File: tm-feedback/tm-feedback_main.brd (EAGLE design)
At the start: 100 x 80 mm, 51 parts

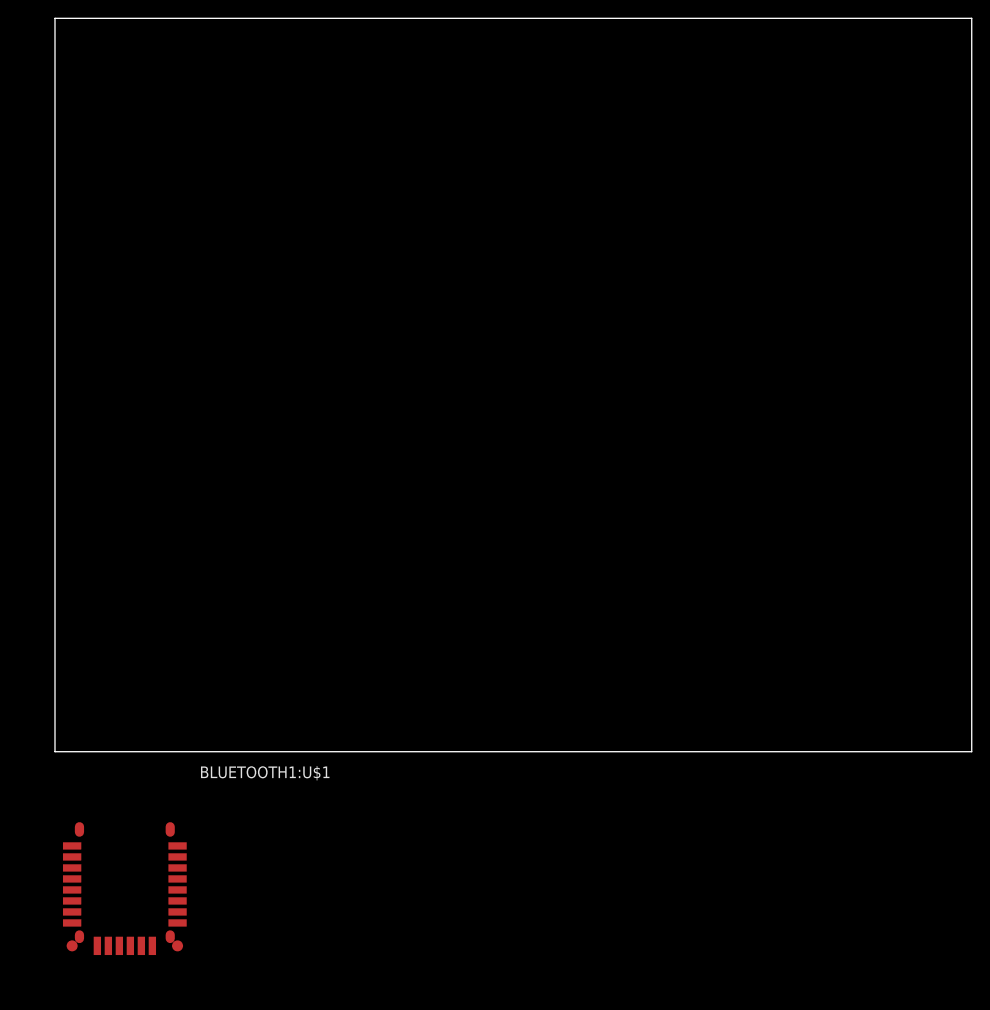
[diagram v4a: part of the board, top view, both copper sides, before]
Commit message: Moved Bluetooth Module to rigth place
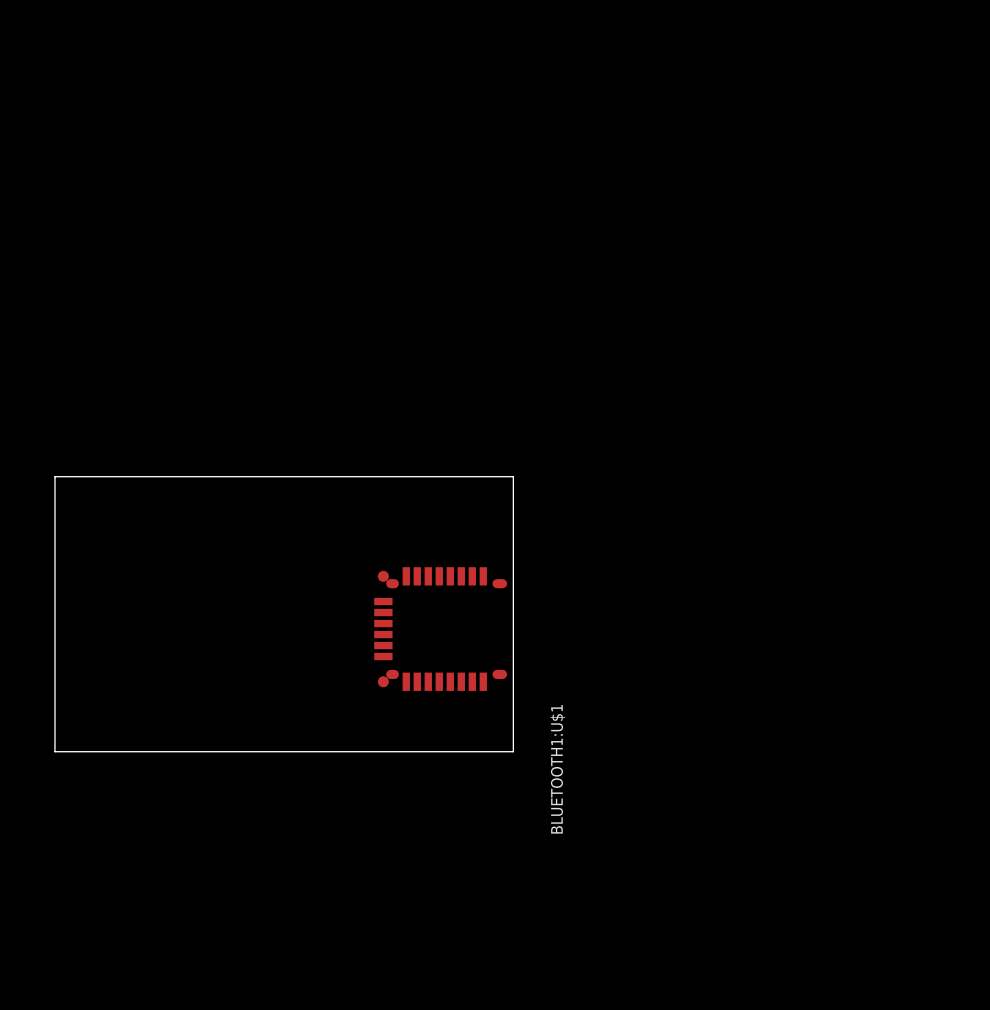
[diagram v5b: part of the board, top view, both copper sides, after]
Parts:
- moved BLUETOOTH1:U$1 45.3 mm to (45.6, 13.4), turned to 270 degrees
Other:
- board size 100 x 80 mm -> 50 x 30 mm
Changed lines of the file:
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@@
 <setting verticaltext="up"/>
 </settings>
-<grid distance="0.05" unitdist="inch" unit="inch" style="lines" multiple="1" display="no" altdistance="0.025" altunitdist="inch" altunit="inch"/>
+<grid distance="1" unitdist="mm" unit="mm" style="lines" multiple="1" display="yes" altdistance="0.1" altunitdist="mm" altunit="mm"/>
 <layers>
 <layer number="1" name="Top" color="4" fill="1" visible="yes" active="yes"/>
@@
 <board>
 <plain>
-<wire x1="0" y1="0" x2="100" y2="0" width="0" layer="20"/>
-<wire x1="100" y1="0" x2="100" y2="80" width="0" layer="20"/>
-<wire x1="100" y1="80" x2="0" y2="80" width="0" layer="20"/>
-<wire x1="0" y1="80" x2="0" y2="0" width="0" layer="20"/>
+<wire x1="0" y1="0" x2="50" y2="0" width="0" layer="20"/>
+<wire x1="50" y1="0" x2="50" y2="30" width="0" layer="20"/>
+<wire x1="50" y1="30" x2="0" y2="30" width="0" layer="20"/>
+<wire x1="0" y1="30" x2="0" y2="0" width="0" layer="20"/>
 </plain>
 <attributes>
@@
 </autorouter>
 <elements>
-<element name="BLUETOOTH1:U$1" library="tactile-music" package="RN4020" value="RN4020" x="7.62" y="-11.43"/>
+<element name="BLUETOOTH1:U$1" library="tactile-music" package="RN4020" value="RN4020" x="45.57" y="13.38" rot="R270"/>
 <element name="POWER_SUPPLY1:LED1" library="led" package="CHIPLED_0805" value="RED" x="-16.51" y="-62.23"/>
 <element name="POWER_SUPPLY1:R1" library="resistor" package="R0805" value="60" x="-16.51" y="-68.58"/>
@@
 <wire x1="-53.34" y1="-118.11" x2="-60.96" y2="-132.08" width="0" layer="19" extent="1-1"/>
 <wire x1="-17.46" y1="-68.58" x2="-53.34" y2="-118.11" width="0" layer="19" extent="1-1"/>
-<wire x1="1.87" y1="-21.18" x2="-17.46" y2="-68.58" width="0" layer="19" extent="1-1"/>
-<wire x1="1.87" y1="-10.28" x2="1.87" y2="-21.18" width="0" layer="19" extent="1-1"/>
-<wire x1="13.37" y1="-21.18" x2="1.87" y2="-21.18" width="0" layer="19" extent="1-1"/>
-<wire x1="13.37" y1="-10.28" x2="13.37" y2="-21.18" width="0" layer="19" extent="1-1"/>
+<wire x1="35.82" y1="7.63" x2="-17.46" y2="-68.58" width="0" layer="19" extent="1-1"/>
+<wire x1="46.72" y1="7.63" x2="35.82" y2="7.63" width="0" layer="19" extent="1-1"/>
+<wire x1="46.72" y1="19.13" x2="46.72" y2="7.63" width="0" layer="19" extent="1-1"/>
+<wire x1="35.82" y1="19.13" x2="46.72" y2="19.13" width="0" layer="19" extent="1-1"/>
 </signal>
 <signal name="BLUETOOTH1:N$6">
@@
 <wire x1="-92.39" y1="-267.97" x2="-92.39" y2="-255.27" width="0" layer="19" extent="1-1"/>
 <wire x1="-92.39" y1="-274.32" x2="-92.39" y2="-267.97" width="0" layer="19" extent="1-1"/>
-<wire x1="13.37" y1="-11.48" x2="-28.26" y2="-83.82" width="0" layer="19" extent="1-1"/>
+<wire x1="45.52" y1="7.63" x2="-28.26" y2="-83.82" width="0" layer="19" extent="1-1"/>
 <wire x1="-96.84" y1="-421.64" x2="-92.39" y2="-274.32" width="0" layer="19" extent="1-1"/>
 <wire x1="-96.84" y1="-426.72" x2="-96.84" y2="-421.64" width="0" layer="19" extent="1-1"/>
@@
 <contactref element="BLUETOOTH1:U$1" pad="14"/>
 <contactref element="MICROCONTROLLER1:U1" pad="27"/>
-<wire x1="9.42" y1="-21.18" x2="-81.93" y2="-234.48" width="0" layer="19" extent="1-1"/>
+<wire x1="35.82" y1="11.58" x2="-81.93" y2="-234.48" width="0" layer="19" extent="1-1"/>
 </signal>
 <signal name="N$6">
 <contactref element="BLUETOOTH1:U$1" pad="18"/>
 <contactref element="MICROCONTROLLER1:U1" pad="41"/>
-<wire x1="13.37" y1="-17.48" x2="-89.23" y2="-227.98" width="0" layer="19" extent="1-1"/>
+<wire x1="39.52" y1="7.63" x2="-89.23" y2="-227.98" width="0" layer="19" extent="1-1"/>
 </signal>
 <signal name="N$7">
 <contactref element="BLUETOOTH1:U$1" pad="5"/>
 <contactref element="MICROCONTROLLER1:U1" pad="5"/>
-<wire x1="1.87" y1="-15.08" x2="-93.33" y2="-232.88" width="0" layer="19" extent="1-1"/>
+<wire x1="41.92" y1="19.13" x2="-93.33" y2="-232.88" width="0" layer="19" extent="1-1"/>
 </signal>
 <signal name="N$8">
 <contactref element="BLUETOOTH1:U$1" pad="6"/>
 <contactref element="MICROCONTROLLER1:U1" pad="4"/>
-<wire x1="1.87" y1="-16.28" x2="-93.33" y2="-232.08" width="0" layer="19" extent="1-1"/>
+<wire x1="40.72" y1="19.13" x2="-93.33" y2="-232.08" width="0" layer="19" extent="1-1"/>
 </signal>
 <signal name="N$9">
 <contactref element="BLUETOOTH1:U$1" pad="15"/>
 <contactref element="MICROCONTROLLER1:U1" pad="38"/>
-<wire x1="10.62" y1="-21.18" x2="-86.83" y2="-227.98" width="0" layer="19" extent="1-1"/>
+<wire x1="35.82" y1="10.38" x2="-86.83" y2="-227.98" width="0" layer="19" extent="1-1"/>
 </signal>
 <signal name="N$10">
@@
 <contactref element="MICROCONTROLLER1:U1" pad="3"/>
 <wire x1="-93.33" y1="-231.28" x2="-70.17" y2="-184.15" width="0" layer="19" extent="1-1"/>
-<wire x1="1.87" y1="-17.48" x2="-70.17" y2="-184.15" width="0" layer="19" extent="1-1"/>
+<wire x1="39.52" y1="19.13" x2="-70.17" y2="-184.15" width="0" layer="19" extent="1-1"/>
 </signal>
 <signal name="N$11">
 <contactref element="BLUETOOTH1:U$1" pad="8"/>
 <contactref element="MICROCONTROLLER1:U1" pad="2"/>
-<wire x1="1.87" y1="-18.68" x2="-93.33" y2="-230.48" width="0" layer="19" extent="1-1"/>
+<wire x1="38.32" y1="19.13" x2="-93.33" y2="-230.48" width="0" layer="19" extent="1-1"/>
 </signal>
 <signal name="N$12">
@@
 <contactref element="MICROCONTROLLER1:U1" pad="44"/>
 <wire x1="-70.17" y1="-189.23" x2="-91.63" y2="-227.98" width="0" layer="19" extent="1-1"/>
-<wire x1="4.62" y1="-21.18" x2="-70.17" y2="-189.23" width="0" layer="19" extent="1-1"/>
+<wire x1="35.82" y1="16.38" x2="-70.17" y2="-189.23" width="0" layer="19" extent="1-1"/>
 </signal>
 <signal name="N$13">
@@
 <contactref element="MICROCONTROLLER1:U1" pad="43"/>
 <wire x1="-76.52" y1="-212.09" x2="-90.83" y2="-227.98" width="0" layer="19" extent="1-1"/>
-<wire x1="5.82" y1="-21.18" x2="-76.52" y2="-212.09" width="0" layer="19" extent="1-1"/>
+<wire x1="35.82" y1="15.18" x2="-76.52" y2="-212.09" width="0" layer="19" extent="1-1"/>
 </signal>
 <signal name="N$14">
@@
 <contactref element="MICROCONTROLLER1:U1" pad="42"/>
 <wire x1="-76.52" y1="-234.95" x2="-90.03" y2="-227.98" width="0" layer="19" extent="1-1"/>
-<wire x1="7.02" y1="-21.18" x2="-90.03" y2="-227.98" width="0" layer="19" extent="1-1"/>
+<wire x1="35.82" y1="13.98" x2="-90.03" y2="-227.98" width="0" layer="19" extent="1-1"/>
 </signal>
 <signal name="N$4">

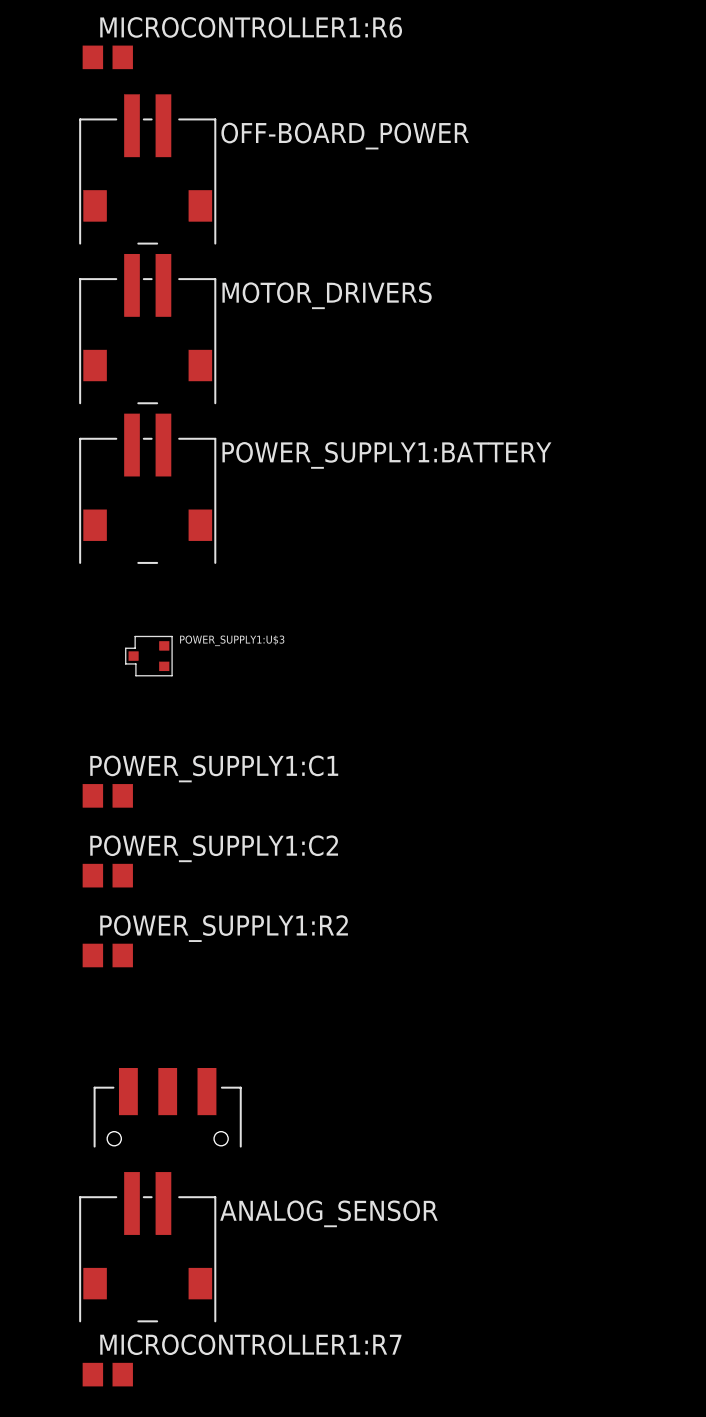
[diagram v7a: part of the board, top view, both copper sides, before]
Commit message: Replaced JST with picoblade
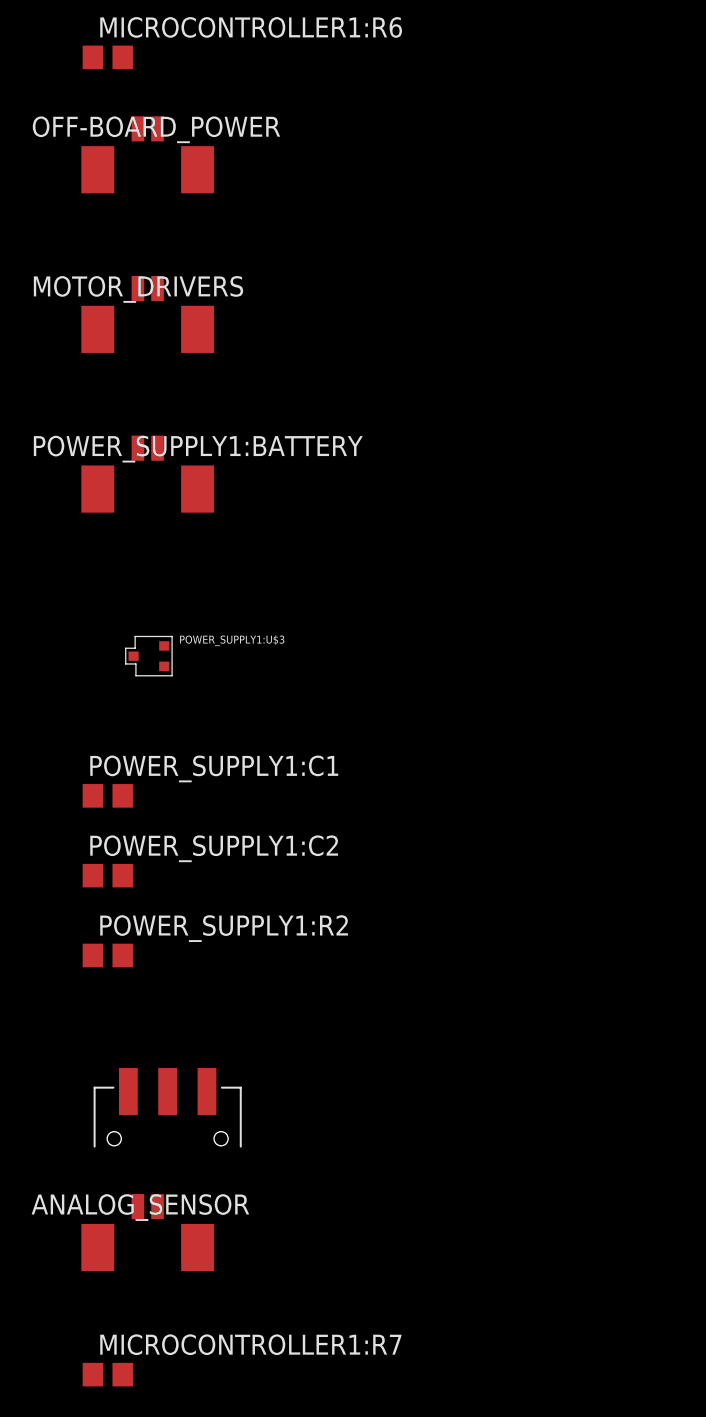
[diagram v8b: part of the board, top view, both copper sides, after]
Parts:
- ANALOG_SENSOR, MOTOR_DRIVERS, OFF-BOARD_POWER, POWER_SUPPLY1:BATTERY: value JST-SMD-2 -> PICOBLADE; device tactile-music:JST-SMD-2 -> tactile-music:PICOBLADE
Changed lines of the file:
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@@
 <element name="MICROCONTROLLER1:LED1" library="led" package="CHIPLED_0805" value="GREEN" x="-92.71" y="-359.41"/>
 <element name="MICROCONTROLLER1:R6" library="resistor" package="R0805" value="60Ω" x="-97.79" y="-369.57"/>
-<element name="OFF-BOARD_POWER" library="tactile-music" package="JST-SMD-2" value="JST-SMD-2" x="-95.25" y="-375.92"/>
-<element name="MOTOR_DRIVERS" library="tactile-music" package="JST-SMD-2" value="JST-SMD-2" x="-95.25" y="-386.08"/>
-<element name="POWER_SUPPLY1:BATTERY" library="tactile-music" package="JST-SMD-2" value="JST-SMD-2" x="-95.25" y="-396.24"/>
+<element name="OFF-BOARD_POWER" library="tactile-music" package="PICOBLADE" value="PICOBLADE" x="-95.25" y="-375.92"/>
+<element name="MOTOR_DRIVERS" library="tactile-music" package="PICOBLADE" value="PICOBLADE" x="-95.25" y="-386.08"/>
+<element name="POWER_SUPPLY1:BATTERY" library="tactile-music" package="PICOBLADE" value="PICOBLADE" x="-95.25" y="-396.24"/>
 <element name="POWER_SUPPLY1:U$3" library="tactile-music" package="SOT323(SC-70)" value="PMF370XN" x="-95.25" y="-407.67"/>
 <element name="POWER_SUPPLY1:C1" library="rcl" package="C0805" value="" x="-97.79" y="-416.56"/>
@@
 <element name="POWER_SUPPLY1:R2" library="resistor" package="R0805" value="60" x="-97.79" y="-426.72"/>
 <element name="POWER_SUPPLY1:POWER_SW" library="tactile-music" package="JS102011SAQN" value="JS102011SAQN" x="-93.98" y="-436.88"/>
-<element name="ANALOG_SENSOR" library="tactile-music" package="JST-SMD-2" value="JST-SMD-2" x="-95.25" y="-444.5"/>
+<element name="ANALOG_SENSOR" library="tactile-music" package="PICOBLADE" value="PICOBLADE" x="-95.25" y="-444.5"/>
 <element name="MICROCONTROLLER1:R7" library="resistor" package="R0805" value="10kΩ" x="-97.79" y="-453.39"/>
 <element name="MICROCONTROLLER1:R8" library="resistor" package="R0805" value="10kΩ" x="-97.79" y="-459.74"/>
@@
 <wire x1="-96.84" y1="-459.74" x2="-96.84" y2="-453.39" width="0" layer="19" extent="1-1"/>
 <wire x1="-96.84" y1="-466.09" x2="-96.84" y2="-459.74" width="0" layer="19" extent="1-1"/>
-<wire x1="-94.25" y1="-373.92" x2="-96.15" y2="-407.67" width="0" layer="19" extent="1-1"/>
-<wire x1="-92.71" y1="-358.36" x2="-94.25" y2="-373.92" width="0" layer="19" extent="1-1"/>
+<wire x1="-94.625" y1="-374.12" x2="-96.15" y2="-407.67" width="0" layer="19" extent="1-1"/>
+<wire x1="-92.71" y1="-358.36" x2="-94.625" y2="-374.12" width="0" layer="19" extent="1-1"/>
 <wire x1="-97.79" y1="-358.36" x2="-92.71" y2="-358.36" width="0" layer="19" extent="1-1"/>
 <wire x1="-97.79" y1="-327.88" x2="-97.79" y2="-358.36" width="0" layer="19" extent="1-1"/>
@@
 <contactref element="MOTOR_DRIVERS" pad="1"/>
 <contactref element="MICROCONTROLLER1:U1" pad="10"/>
-<wire x1="-93.33" y1="-236.88" x2="-96.25" y2="-384.08" width="0" layer="19" extent="1-1"/>
+<wire x1="-93.33" y1="-236.88" x2="-95.875" y2="-384.28" width="0" layer="19" extent="1-1"/>
 </signal>
 <signal name="N$5">
@@
 <contactref element="POWER_SUPPLY1:U$1" pad="1"/>
 <contactref element="POWER_SUPPLY1:POWER_SW" pad="3"/>
-<wire x1="-96.84" y1="-416.56" x2="-96.25" y2="-373.92" width="0" layer="19" extent="1-1"/>
+<wire x1="-96.84" y1="-416.56" x2="-95.875" y2="-374.12" width="0" layer="19" extent="1-1"/>
 <wire x1="-91.48" y1="-435.38" x2="-96.84" y2="-416.56" width="0" layer="19" extent="1-1"/>
-<wire x1="-59.7916" y1="-138.7602" x2="-96.25" y2="-373.92" width="0" layer="19" extent="1-1"/>
+<wire x1="-59.7916" y1="-138.7602" x2="-95.875" y2="-374.12" width="0" layer="19" extent="1-1"/>
 <wire x1="-16.51" y1="-63.28" x2="-59.7916" y2="-138.7602" width="0" layer="19" extent="1-1"/>
 </signal>
@@
 <contactref element="POWER_SUPPLY1:U$3" pad="1"/>
 <contactref element="POWER_SUPPLY1:POWER_SW" pad="2"/>
-<wire x1="-94.25" y1="-394.24" x2="-94.2" y2="-408.32" width="0" layer="19" extent="1-1"/>
+<wire x1="-94.625" y1="-394.44" x2="-94.2" y2="-408.32" width="0" layer="19" extent="1-1"/>
 <wire x1="-93.98" y1="-435.38" x2="-94.2" y2="-408.32" width="0" layer="19" extent="1-1"/>
 </signal>
@@
 <contactref element="POWER_SUPPLY1:BATTERY" pad="1"/>
 <contactref element="POWER_SUPPLY1:U$3" pad="2"/>
-<wire x1="-96.25" y1="-394.24" x2="-94.2" y2="-407.02" width="0" layer="19" extent="1-1"/>
+<wire x1="-95.875" y1="-394.44" x2="-94.2" y2="-407.02" width="0" layer="19" extent="1-1"/>
 </signal>
 <signal name="+3V3">
@@
 <contactref element="MICROCONTROLLER1:U1" pad="8"/>
 <contactref element="MOTOR_DRIVERS" pad="2"/>
-<wire x1="-93.33" y1="-235.28" x2="-94.25" y2="-384.08" width="0" layer="19" extent="1-1"/>
+<wire x1="-93.33" y1="-235.28" x2="-94.625" y2="-384.28" width="0" layer="19" extent="1-1"/>
 </signal>
 <signal name="N$15">
 <contactref element="ANALOG_SENSOR" pad="1"/>
 <contactref element="MICROCONTROLLER1:U1" pad="23"/>
-<wire x1="-96.25" y1="-442.5" x2="-81.93" y2="-237.68" width="0" layer="19" extent="1-1"/>
+<wire x1="-95.875" y1="-442.7" x2="-81.93" y2="-237.68" width="0" layer="19" extent="1-1"/>
 </signal>
 <signal name="N$16">
 <contactref element="ANALOG_SENSOR" pad="2"/>
 <contactref element="MICROCONTROLLER1:U1" pad="24"/>
-<wire x1="-94.25" y1="-442.5" x2="-81.93" y2="-236.88" width="0" layer="19" extent="1-1"/>
+<wire x1="-94.625" y1="-442.7" x2="-81.93" y2="-236.88" width="0" layer="19" extent="1-1"/>
 </signal>
 <signal name="MICROCONTROLLER1:N$5">
